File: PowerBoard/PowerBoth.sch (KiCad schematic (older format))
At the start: 0 parts

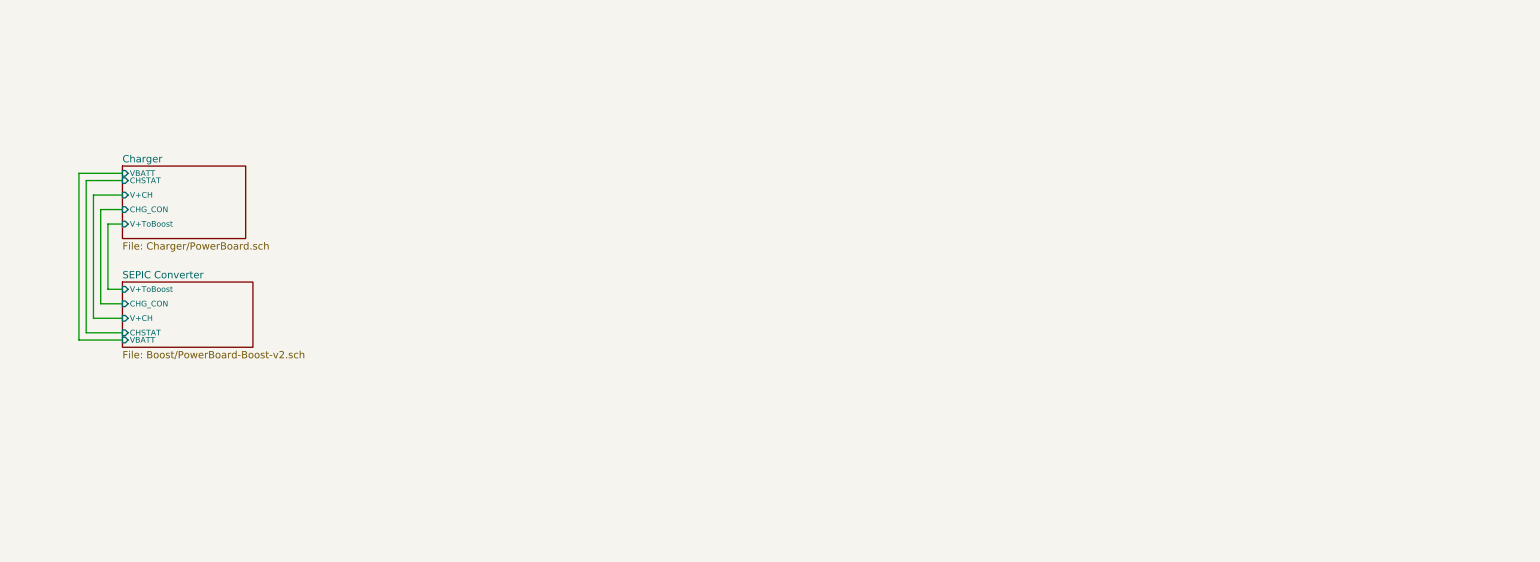
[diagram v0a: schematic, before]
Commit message: Replacing the SEPIC converter.
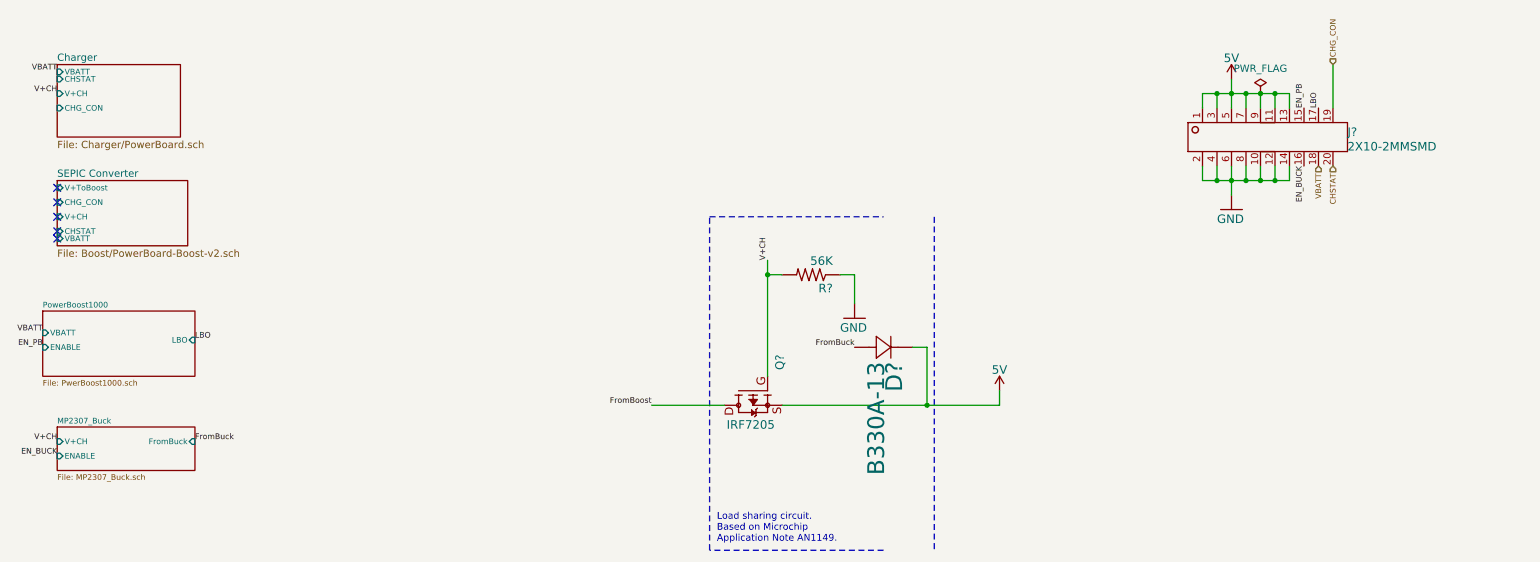
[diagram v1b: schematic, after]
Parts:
- added D?: B330A-13, PowerBoard:SMA-M, symbol PowerBoth-rescue:B330A-13-PowerBoard-eagle-import
- added J?: 2X10-2MMSMD, PowerBoard-Boost-v2:2X10-2MM, symbol PowerBoth-rescue:2X10-2MMSMD-PowerBoard-Boost-v2-eagle-import
- added Q?: IRF7205, PowerBoard:8SOIC, symbol PowerBoth-rescue:IRF7205-PowerBoard-eagle-import
- added R?: 56K, PowerBoard:1206, symbol PowerBoth-rescue:RESISTOR1206-PowerBoard-eagle-import
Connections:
- new net: D?.1, Q?.1 (S), Q?.2 (S), Q?.3 (S)
- new net: J?.1 (P$1), J?.11 (P$11), J?.13 (P$13), J?.3 (P$3), J?.5 (P$5), J?.7 (P$7), J?.9 (P$9)
- new net: J?.10 (P$10), J?.12 (P$12), J?.14 (P$14), J?.2 (P$2), J?.4 (P$4), J?.6 (P$6), J?.8 (P$8)
- new net CHG_CON: J?.19 (P$19)
- new net CHSTAT: J?.20 (P$20)
- new net EN_BUCK: J?.16 (P$16)
- new net EN_PB: J?.15 (P$15)
- new net FromBoost: Q?.5 (D), Q?.6 (D), Q?.7 (D), Q?.8 (D)
- new net FromBuck: D?.2
- new net LBO: J?.17 (P$17)
- new net V+CH: Q?.4 (G), R?.2
- new net VBATT: J?.18 (P$18)
- no-connect marks 0 -> 5
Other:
- note added: "Load sharing circuit.\nBased on Microchip\nApplication Note AN1149."

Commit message: Replacing the SEPIC converter.
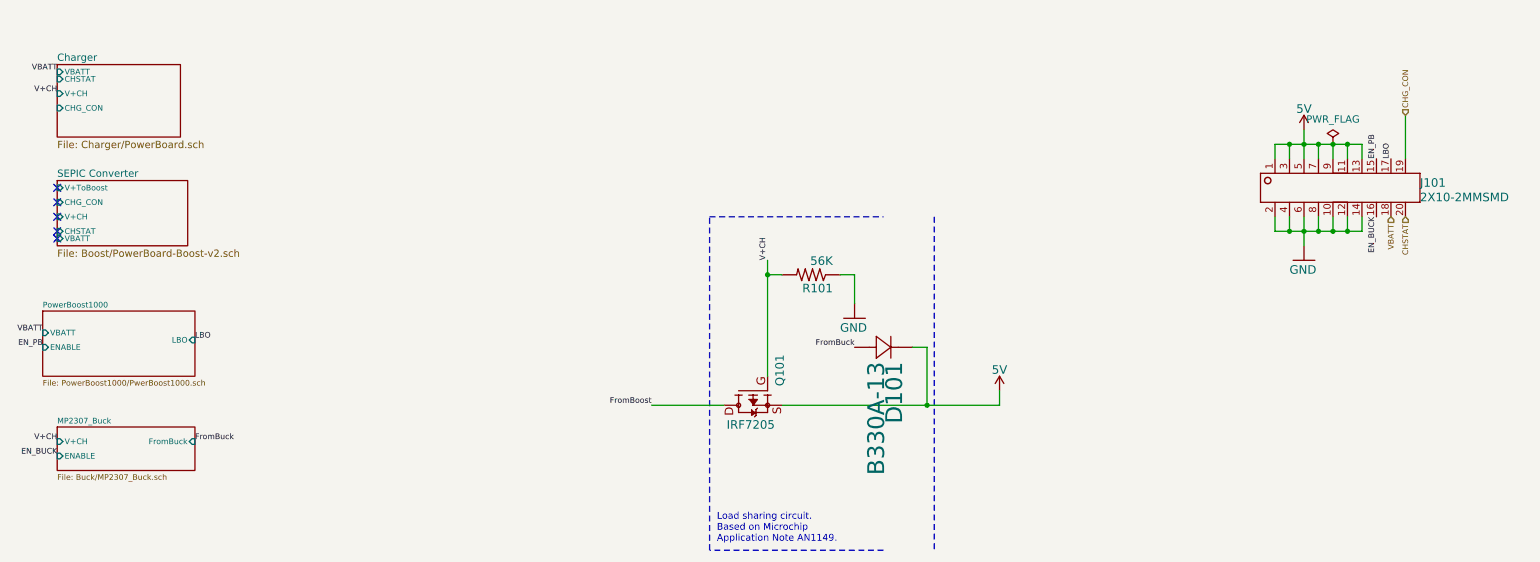
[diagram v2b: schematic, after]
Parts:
- gave numbers to parts that had none: 4
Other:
- moved on the sheet: J101
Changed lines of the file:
@@
 F0 "Charger" 50
 F1 "Charger/PowerBoard.sch" 50
-F3 "CHG_CON" I L 1000 950 39
-F4 "V+CH" I L 1000 850 39
-F5 "CHSTAT" I L 1000 750 39
-F6 "VBATT" I L 1000 700 39
+F2 "CHG_CON" I L 1000 950 39
+F3 "V+CH" I L 1000 850 39
+F4 "CHSTAT" I L 1000 750 39
+F5 "VBATT" I L 1000 700 39
 $EndSheet
 $Sheet
@@
 F6 "VBATT" I L 1000 1850 39
 $EndSheet
-$Sheet
-S 900  2350 1050 450
-U 5ED79595
-F0 "PowerBoost1000" 39
-F1 "PwerBoost1000.sch" 39
-F2 "LBO" I R 1950 2550 39
-F3 "VBATT" I L 900 2500 39
-F4 "ENABLE" I L 900 2600 39
-$EndSheet
-$Sheet
-S 1000 3150 950  300
-U 5EDA5AF4
-F0 "MP2307_Buck" 39
-F1 "MP2307_Buck.sch" 39
-F2 "V+CH" I L 1000 3250 39
-F3 "FromBuck" I R 1950 3250 39
-F4 "ENABLE" I L 1000 3350 39
-$EndSheet
 Wire Wire Line
 	6500 2100 6500 2300
@@
 P 6200 2100
 AR Path="/5EC9FE80/5EDB5107" Ref="R?"  Part="1"
-AR Path="/5EDB5107" Ref="R?"  Part="1"
-F 0 "R?" H 6050 2159 59  0000 L BNN
+AR Path="/5EDB5107" Ref="R101"  Part="1"
+F 0 "R101" H 6050 2159 59  0000 L BNN
 F 1 "56K" H 6050 1970 59  0000 L BNN
 F 2 "PowerBoard:1206" H 6200 2100 50  0001 C CNN
@@
 P 6500 2400
 AR Path="/5EC9FE80/5EDB510D" Ref="#GND?"  Part="1"
-AR Path="/5EDB510D" Ref="#GND?"  Part="1"
-F 0 "#GND?" H 6500 2400 50  0001 C CNN
+AR Path="/5EDB510D" Ref="#GND0101"  Part="1"
+F 0 "#GND0101" H 6500 2400 50  0001 C CNN
 F 1 "GND" H 6400 2300 59  0000 L BNN
 F 2 "" H 6500 2400 50  0001 C CNN
@@
 P 5800 3000
 AR Path="/5EC9FE80/5EDB5114" Ref="Q?"  Part="1"
-AR Path="/5EDB5114" Ref="Q?"  Part="1"
-F 0 "Q?" H 5450 2850 59  0000 L TNN
+AR Path="/5EDB5114" Ref="Q101"  Part="1"
+F 0 "Q101" H 5450 2850 59  0000 L TNN
 F 1 "IRF7205" V 5900 2850 59  0000 L TNN
 F 2 "PowerBoard:8SOIC" H 5800 3000 50  0001 C CNN
@@
 P 6500 2600
 AR Path="/5EC9FE80/5EDB511A" Ref="D?"  Part="1"
-AR Path="/5EDB511A" Ref="D?"  Part="1"
-F 0 "D?" H 6600 2806 116 0000 L BNN
+AR Path="/5EDB511A" Ref="D101"  Part="1"
+F 0 "D101" H 6600 2806 116 0000 L BNN
 F 1 "B330A-13" H 6600 2682 116 0000 L BNN
 F 2 "PowerBoard:SMA-M" H 6500 2600 50  0001 C CNN
@@
 FromBuck
 Wire Wire Line
-	8900 1350 8900 1450
-Wire Wire Line
-	8900 1450 9000 1450
-Wire Wire Line
-	9000 1450 9100 1450
-Wire Wire Line
-	9100 1450 9100 1550
-Wire Wire Line
-	9000 1350 9000 1450
-Wire Wire Line
-	9100 1350 9100 1450
-Wire Wire Line
-	9200 1350 9200 1450
-Wire Wire Line
-	9200 1450 9100 1450
-Wire Wire Line
-	9200 1450 9300 1450
-Wire Wire Line
-	9300 1450 9300 1350
-Wire Wire Line
-	9300 1450 9400 1450
-Wire Wire Line
-	9400 1450 9400 1350
-Wire Wire Line
-	9400 1450 9500 1450
-Wire Wire Line
-	9500 1450 9500 1350
-Connection ~ 9000 1450
-Connection ~ 9100 1450
-Connection ~ 9200 1450
-Connection ~ 9300 1450
-Connection ~ 9400 1450
-Wire Wire Line
-	9800 950  9800 650
-Wire Wire Line
-	8900 950  8900 850
-Wire Wire Line
-	8900 850  9000 850
-Wire Wire Line
-	9000 850  9100 850
-Wire Wire Line
-	9100 850  9100 750
-Wire Wire Line
-	9000 950  9000 850
-Wire Wire Line
-	9100 950  9100 850
-Wire Wire Line
-	9200 950  9200 850
-Wire Wire Line
-	9200 850  9100 850
-Wire Wire Line
-	9300 950  9300 850
-Wire Wire Line
-	9300 850  9200 850
-Wire Wire Line
-	9400 950  9400 850
-Wire Wire Line
-	9400 850  9300 850
-Wire Wire Line
-	9500 950  9500 850
-Wire Wire Line
-	9500 850  9400 850
-Connection ~ 9000 850
-Connection ~ 9100 850
-Connection ~ 9200 850
-Connection ~ 9300 850
-Connection ~ 9400 850
-$Comp
-L PowerBoth-rescue:2X10-2MMSMD-PowerBoard-Boost-v2-eagle-import J?
+	9400 1700 9400 1800
+Wire Wire Line
+	9400 1800 9500 1800
+Wire Wire Line
+	9500 1800 9600 1800
+Wire Wire Line
+	9600 1800 9600 1900
+Wire Wire Line
+	9500 1700 9500 1800
+Wire Wire Line
+	9600 1700 9600 1800
+Wire Wire Line
+	9700 1700 9700 1800
+Wire Wire Line
+	9700 1800 9600 1800
+Wire Wire Line
+	9700 1800 9800 1800
+Wire Wire Line
+	9800 1800 9800 1700
+Wire Wire Line
+	9800 1800 9900 1800
+Wire Wire Line
+	9900 1800 9900 1700
+Wire Wire Line
+	9900 1800 10000 1800
+Wire Wire Line
+	10000 1800 10000 1700
+Connection ~ 9500 1800
+Connection ~ 9600 1800
+Connection ~ 9700 1800
+Connection ~ 9800 1800
+Connection ~ 9900 1800
+Wire Wire Line
+	10300 1300 10300 1000
+Wire Wire Line
+	9400 1300 9400 1200
+Wire Wire Line
+	9400 1200 9500 1200
+Wire Wire Line
+	9500 1200 9600 1200
+Wire Wire Line
+	9600 1200 9600 1100
+Wire Wire Line
+	9500 1300 9500 1200
+Wire Wire Line
+	9600 1300 9600 1200
+Wire Wire Line
+	9700 1300 9700 1200
+Wire Wire Line
+	9700 1200 9600 1200
+Wire Wire Line
+	9800 1300 9800 1200
+Wire Wire Line
+	9800 1200 9700 1200
+Wire Wire Line
+	9900 1300 9900 1200
+Wire Wire Line
+	9900 1200 9800 1200
+Wire Wire Line
+	10000 1300 10000 1200
+Wire Wire Line
+	10000 1200 9900 1200
+Connection ~ 9500 1200
+Connection ~ 9600 1200
+Connection ~ 9700 1200
+Connection ~ 9800 1200
+Connection ~ 9900 1200
+$Comp
+L PowerBoth-rescue:2X10-2MMSMD-PowerBoard-Boost-v2-eagle-import J101
 U 1 1 5EDBF0DD
-P 8800 1250
-AR Path="/5EDBF0DD" Ref="J?"  Part="1"
+P 9300 1600
+AR Path="/5EDBF0DD" Ref="J101"  Part="1"
 AR Path="/5E8AAE5F/5EDBF0DD" Ref="J?"  Part="1"
 AR Path="/5ECA2372/5E8AAE5F/5EDBF0DD" Ref="J?"  Part="1"
 AR Path="/5ECA2372/5EDBF0DD" Ref="J?"  Part="1"
-F 0 "J?" H 9900 1350 59  0000 L BNN
-F 1 "2X10-2MMSMD" H 9900 1250 59  0000 L BNN
-F 2 "PowerBoard-Boost-v2:2X10-2MM" H 8800 1250 50  0001 C CNN
-F 3 "" H 8800 1250 50  0001 C CNN
-	1    8800 1250
-	1    0    0    -1
-$EndComp
-$Comp
-L PowerBoth-rescue:5V-PowerBoard-Boost-v2-eagle-import #SUPPLY?
+F 0 "J101" H 10400 1700 59  0000 L BNN
+F 1 "2X10-2MMSMD" H 10400 1600 59  0000 L BNN
+F 2 "PowerBoard-Boost-v2:2X10-2MM" H 9300 1600 50  0001 C CNN
+F 3 "" H 9300 1600 50  0001 C CNN
+	1    9300 1600
+	1    0    0    -1
+$EndComp
+$Comp
+L PowerBoth-rescue:5V-PowerBoard-Boost-v2-eagle-import #SUPPLY0101
 U 1 1 5EDBF0E3
-P 9100 750
-AR Path="/5EDBF0E3" Ref="#SUPPLY?"  Part="1"
+P 9600 1100
+AR Path="/5EDBF0E3" Ref="#SUPPLY0101"  Part="1"
 AR Path="/5E8AAE5F/5EDBF0E3" Ref="#SUPPLY?"  Part="1"
 AR Path="/5ECA2372/5E8AAE5F/5EDBF0E3" Ref="#SUPPLY?"  Part="1"
 AR Path="/5ECA2372/5EDBF0E3" Ref="#SUPPLY?"  Part="1"
-F 0 "#SUPPLY?" H 9100 750 50  0001 C CNN
-F 1 "5V" H 9100 860 59  0000 C BNN
-F 2 "" H 9100 750 50  0001 C CNN
-F 3 "" H 9100 750 50  0001 C CNN
-	1    9100 750
-	1    0    0    -1
-$EndComp
-$Comp
-L PowerBoth-rescue:GND-PowerBoard-Boost-v2-eagle-import #GND?
+F 0 "#SUPPLY0101" H 9600 1100 50  0001 C CNN
+F 1 "5V" H 9600 1210 59  0000 C BNN
+F 2 "" H 9600 1100 50  0001 C CNN
+F 3 "" H 9600 1100 50  0001 C CNN
+	1    9600 1100
+	1    0    0    -1
+$EndComp
+$Comp
+L PowerBoth-rescue:GND-PowerBoard-Boost-v2-eagle-import #GND0102
 U 1 1 5EDBF0E9
-P 9100 1650
-AR Path="/5EDBF0E9" Ref="#GND?"  Part="1"
+P 9600 2000
+AR Path="/5EDBF0E9" Ref="#GND0102"  Part="1"
 AR Path="/5E8AAE5F/5EDBF0E9" Ref="#GND?"  Part="1"
 AR Path="/5ECA2372/5E8AAE5F/5EDBF0E9" Ref="#GND?"  Part="1"
 AR Path="/5ECA2372/5EDBF0E9" Ref="#GND?"  Part="1"
-F 0 "#GND?" H 9100 1650 50  0001 C CNN
-F 1 "GND" H 9000 1550 59  0000 L BNN
-F 2 "" H 9100 1650 50  0001 C CNN
-F 3 "" H 9100 1650 50  0001 C CNN
-	1    9100 1650
-	1    0    0    -1
-$EndComp
-Text HLabel 9800 650  1    39   Input ~ 0
+F 0 "#GND0102" H 9600 2000 50  0001 C CNN
+F 1 "GND" H 9500 1900 59  0000 L BNN
+F 2 "" H 9600 2000 50  0001 C CNN
+F 3 "" H 9600 2000 50  0001 C CNN
+	1    9600 2000
+	1    0    0    -1
+$EndComp
+Text HLabel 10300 1000 1    39   Input ~ 0
 CHG_CON
-Text HLabel 9800 1350 3    39   Input ~ 0
+Text HLabel 10300 1700 3    39   Input ~ 0
 CHSTAT
-Text HLabel 9700 1350 3    39   Input ~ 0
+Text HLabel 10200 1700 3    39   Input ~ 0
 VBATT
 $Comp
 L power:PWR_FLAG #FLG?
 U 1 1 5EDBF0F4
-P 9300 850
+P 9800 1200
 AR Path="/5ECA2372/5EDBF0F4" Ref="#FLG?"  Part="1"
-AR Path="/5EDBF0F4" Ref="#FLG?"  Part="1"
-F 0 "#FLG?" H 9300 925 50  0001 C CNN
-F 1 "PWR_FLAG" H 9300 1023 50  0000 C CNN
-F 2 "" H 9300 850 50  0001 C CNN
-F 3 "~" H 9300 850 50  0001 C CNN
-	1    9300 850
-	1    0    0    -1
-$EndComp
-$Comp
-L PowerBoth-rescue:5V-PowerBoard-Boost-v2-eagle-import #SUPPLY?
+AR Path="/5EDBF0F4" Ref="#FLG0103"  Part="1"
+F 0 "#FLG0103" H 9800 1275 50  0001 C CNN
+F 1 "PWR_FLAG" H 9800 1373 50  0000 C CNN
+F 2 "" H 9800 1200 50  0001 C CNN
+F 3 "~" H 9800 1200 50  0001 C CNN
+	1    9800 1200
+	1    0    0    -1
+$EndComp
+$Comp
+L PowerBoth-rescue:5V-PowerBoard-Boost-v2-eagle-import #SUPPLY0102
 U 1 1 5EDBFBD2
 P 7500 2900
-AR Path="/5EDBFBD2" Ref="#SUPPLY?"  Part="1"
+AR Path="/5EDBFBD2" Ref="#SUPPLY0102"  Part="1"
 AR Path="/5E8AAE5F/5EDBFBD2" Ref="#SUPPLY?"  Part="1"
 AR Path="/5ECA2372/5E8AAE5F/5EDBFBD2" Ref="#SUPPLY?"  Part="1"
 AR Path="/5ECA2372/5EDBFBD2" Ref="#SUPPLY?"  Part="1"
-F 0 "#SUPPLY?" H 7500 2900 50  0001 C CNN
+F 0 "#SUPPLY0102" H 7500 2900 50  0001 C CNN
 F 1 "5V" H 7500 3010 59  0000 C BNN
 F 2 "" H 7500 2900 50  0001 C CNN
@@
 Text Label 5900 2000 1    39   ~ 0
 V+CH
-Text Label 9700 950  1    39   ~ 0
+Text Label 10200 1300 1    39   ~ 0
 LBO
 Text Label 1000 700  2    39   ~ 0
@@
 Text Label 900  2600 2    39   ~ 0
 EN_PB
-Text Label 9600 950  1    39   ~ 0
+Text Label 10100 1300 1    39   ~ 0
 EN_PB
 Text Label 1000 3350 2    39   ~ 0
 EN_BUCK
-Text Label 9600 1350 3    39   ~ 0
+Text Label 10100 1700 3    39   ~ 0
 EN_BUCK
 NoConn ~ 1000 1500
@@
 NoConn ~ 1000 1850
 NoConn ~ 1000 1800
+$Sheet
+S 1000 3150 950  300
+U 5EDA5AF4
+F0 "MP2307_Buck" 39
+F1 "Buck/MP2307_Buck.sch" 39
+F2 "V+CH" I L 1000 3250 39
+F3 "FromBuck" I R 1950 3250 39
+F4 "ENABLE" I L 1000 3350 39
+$EndSheet
+$Sheet
+S 900  2350 1050 450
+U 5ED79595
+F0 "PowerBoost1000" 39
+F1 "PowerBoost1000/PwerBoost1000.sch" 39
+F2 "LBO" I R 1950 2550 39
+F3 "VBATT" I L 900 2500 39
+F4 "ENABLE" I L 900 2600 39
+$EndSheet
 $EndSCHEMATC

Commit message: Separating the power board branch.
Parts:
- D101: DigiKey (none) -> B330B-13-F; LCSC Part Number (none) -> C110485
- J101: footprint PowerBoard-Boost-v2:2X10-2MM -> MarcoK:2X10-2MM; DigiKey (none) -> NPPN102GFNP-RC
- Q101: DigiKey (none) -> IRF7205TRPBF
- R101: DigiKey (none) -> CRCW120656K0FKEA; LCSC Part Number (none) -> C18029
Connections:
- net EN_BUCK: no longer J101.16 (P$16)
- no-connect marks 5 -> 1
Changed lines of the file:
@@
 $Descr A4 11693 8268
 encoding utf-8
-Sheet 1 5
+Sheet 1 4
 Title "CR101 Power Board"
 Date "2020-06-01"
@@
 F5 "VBATT" I L 1000 700 39
 $EndSheet
-$Sheet
-S 1000 1450 900  450
-U 5ECA2372
-F0 "SEPIC Converter" 50
-F1 "Boost/PowerBoard-Boost-v2.sch" 50
-F2 "CHSTAT" I L 1000 1800 39
-F3 "CHG_CON" I L 1000 1600 39
-F4 "V+ToBoost" I L 1000 1500 39
-F5 "V+CH" I L 1000 1700 39
-F6 "VBATT" I L 1000 1850 39
-$EndSheet
 Wire Wire Line
 	6500 2100 6500 2300
-Wire Wire Line
-	5600 3000 5100 3000
 $Comp
 L PowerBoth-rescue:RESISTOR1206-PowerBoard-eagle-import R?
@@
 F 2 "PowerBoard:1206" H 6200 2100 50  0001 C CNN
 F 3 "" H 6200 2100 50  0001 C CNN
+F 4 "CRCW120656K0FKEA" H 6200 2100 50  0001 C CNN "DigiKey"
+F 5 "C18029" H 6200 2100 50  0001 C CNN "LCSC Part Number"
 	1    6200 2100
 	-1   0    0    1
@@
 F 3 "" H 5800 3000 50  0001 C CNN
 F 4 "C55419" H 5800 3000 50  0001 C CNN "LCSC Part Number"
+F 5 "IRF7205TRPBF" H 5800 3000 50  0001 C CNN "DigiKey"
 	1    5800 3000
 	0    -1   1    0
@@
 F 2 "PowerBoard:SMA-M" H 6500 2600 50  0001 C CNN
 F 3 "" H 6500 2600 50  0001 C CNN
+F 4 "B330B-13-F" H 6500 2600 50  0001 C CNN "DigiKey"
+F 5 "C110485" H 6500 2600 50  0001 C CNN "LCSC Part Number"
 	1    6500 2600
 	0    1    1    0
@@
 Text Notes 5550 3950 0    47   ~ 0
 Load sharing circuit.\nBased on Microchip\nApplication Note AN1149.
-Text Label 5100 3000 2    39   ~ 0
+Text Label 5600 3000 2    39   ~ 0
 FromBoost
 Wire Wire Line
@@
 Text Label 6500 2600 2    39   ~ 0
 FromBuck
-Text Label 1950 3250 0    39   ~ 0
+Text Label 1950 1550 0    39   ~ 0
 FromBuck
 Wire Wire Line
@@
 Connection ~ 9900 1800
 Wire Wire Line
-	10300 1300 10300 1000
-Wire Wire Line
 	9400 1300 9400 1200
 Wire Wire Line
@@
 Wire Wire Line
 	9500 1200 9600 1200
-Wire Wire Line
-	9600 1200 9600 1100
 Wire Wire Line
 	9500 1300 9500 1200
@@
 F 0 "J101" H 10400 1700 59  0000 L BNN
 F 1 "2X10-2MMSMD" H 10400 1600 59  0000 L BNN
-F 2 "PowerBoard-Boost-v2:2X10-2MM" H 9300 1600 50  0001 C CNN
+F 2 "MarcoK:2X10-2MM" H 9300 1600 50  0001 C CNN
 F 3 "" H 9300 1600 50  0001 C CNN
+F 4 "NPPN102GFNP-RC" H 9300 1600 50  0001 C CNN "DigiKey"
 	1    9300 1600
 	1    0    0    -1
@@
 	1    0    0    -1
 $EndComp
-Text HLabel 10300 1000 1    39   Input ~ 0
-CHG_CON
-Text HLabel 10300 1700 3    39   Input ~ 0
-CHSTAT
-Text HLabel 10200 1700 3    39   Input ~ 0
-VBATT
-$Comp
-L power:PWR_FLAG #FLG?
-U 1 1 5EDBF0F4
-P 9800 1200
-AR Path="/5ECA2372/5EDBF0F4" Ref="#FLG?"  Part="1"
-AR Path="/5EDBF0F4" Ref="#FLG0103"  Part="1"
-F 0 "#FLG0103" H 9800 1275 50  0001 C CNN
-F 1 "PWR_FLAG" H 9800 1373 50  0000 C CNN
-F 2 "" H 9800 1200 50  0001 C CNN
-F 3 "~" H 9800 1200 50  0001 C CNN
-	1    9800 1200
-	1    0    0    -1
-$EndComp
 $Comp
 L PowerBoth-rescue:5V-PowerBoard-Boost-v2-eagle-import #SUPPLY0102
@@
 Wire Wire Line
 	7000 3000 7500 3000
-Text Label 1950 2550 0    39   ~ 0
+Text Label 2000 2150 0    39   ~ 0
 LBO
-Text Label 1000 3250 2    39   ~ 0
+Text Label 1000 1550 2    39   ~ 0
 V+CH
 Text Label 1000 850  2    39   ~ 0
 V+CH
-NoConn ~ 1000 1700
 Text Label 5900 2000 1    39   ~ 0
 V+CH
@@
 Text Label 1000 700  2    39   ~ 0
 VBATT
-Text Label 900  2500 2    39   ~ 0
+Text Label 950  2100 2    39   ~ 0
 VBATT
-Text Label 900  2600 2    39   ~ 0
+Text Label 950  2200 2    39   ~ 0
 EN_PB
 Text Label 10100 1300 1    39   ~ 0
 EN_PB
-Text Label 1000 3350 2    39   ~ 0
+Text Label 1000 1650 2    39   ~ 0
 EN_BUCK
-Text Label 10100 1700 3    39   ~ 0
-EN_BUCK
-NoConn ~ 1000 1500
-NoConn ~ 1000 1600
-NoConn ~ 1000 1850
-NoConn ~ 1000 1800
 $Sheet
-S 1000 3150 950  300
+S 1000 1450 950  300
 U 5EDA5AF4
 F0 "MP2307_Buck" 39
 F1 "Buck/MP2307_Buck.sch" 39
-F2 "V+CH" I L 1000 3250 39
-F3 "FromBuck" I R 1950 3250 39
-F4 "ENABLE" I L 1000 3350 39
+F2 "V+CH" I L 1000 1550 39
+F3 "FromBuck" I R 1950 1550 39
+F4 "ENABLE" I L 1000 1650 39
 $EndSheet
+Text Label 1000 750  2    39   ~ 0
+CHSTAT
+Text Label 1000 950  2    39   ~ 0
+CHG_CON
+Text Label 10300 1300 1    39   ~ 0
+CHG_CON
+Text Label 10300 1700 3    39   ~ 0
+CHSTAT
+Text Label 10200 1700 3    39   ~ 0
+VBATT
+Wire Wire Line
+	9600 1200 9600 1100
 $Sheet
-S 900  2350 1050 450
+S 950  1950 1050 450
 U 5ED79595
 F0 "PowerBoost1000" 39
 F1 "PowerBoost1000/PwerBoost1000.sch" 39
-F2 "LBO" I R 1950 2550 39
-F3 "VBATT" I L 900 2500 39
-F4 "ENABLE" I L 900 2600 39
+F2 "LBO" I R 2000 2150 39
+F3 "VBATT" I L 950 2100 39
+F4 "ENABLE" I L 950 2200 39
+F5 "FromBoost" I R 2000 2250 39
 $EndSheet
+Text Label 2000 2250 0    39   ~ 0
+FromBoost
+NoConn ~ 10100 1700
 $EndSCHEMATC
